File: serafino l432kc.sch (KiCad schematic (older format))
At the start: 28 parts

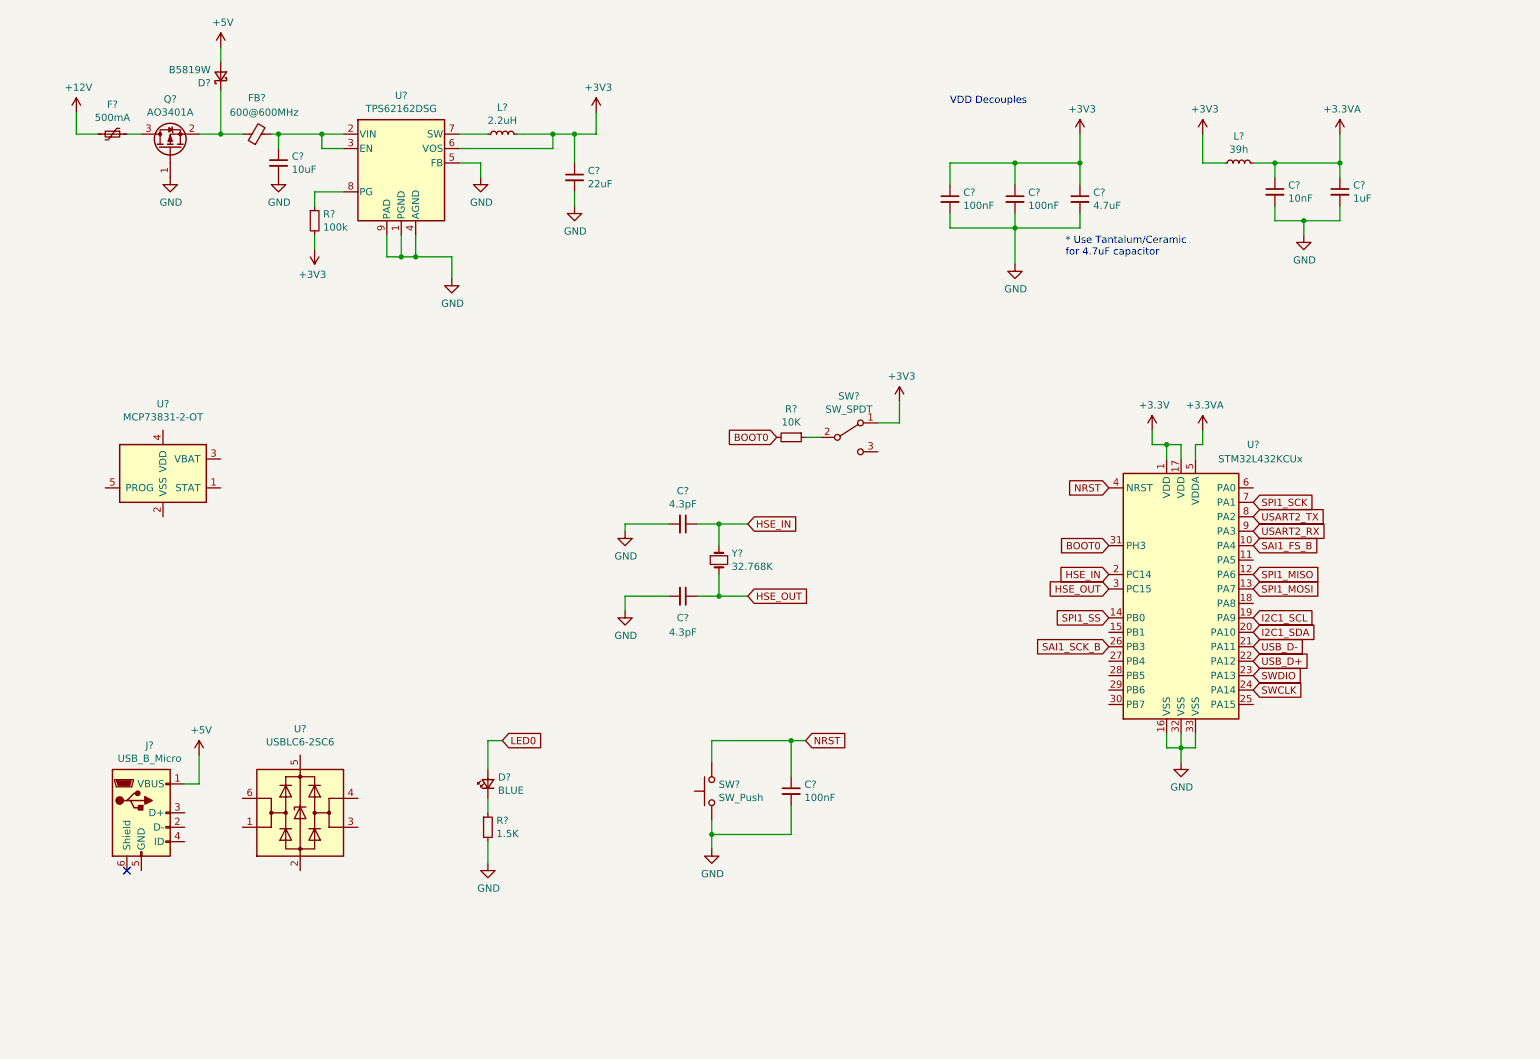
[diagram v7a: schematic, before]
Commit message: Upgrade to high effiency buck converter
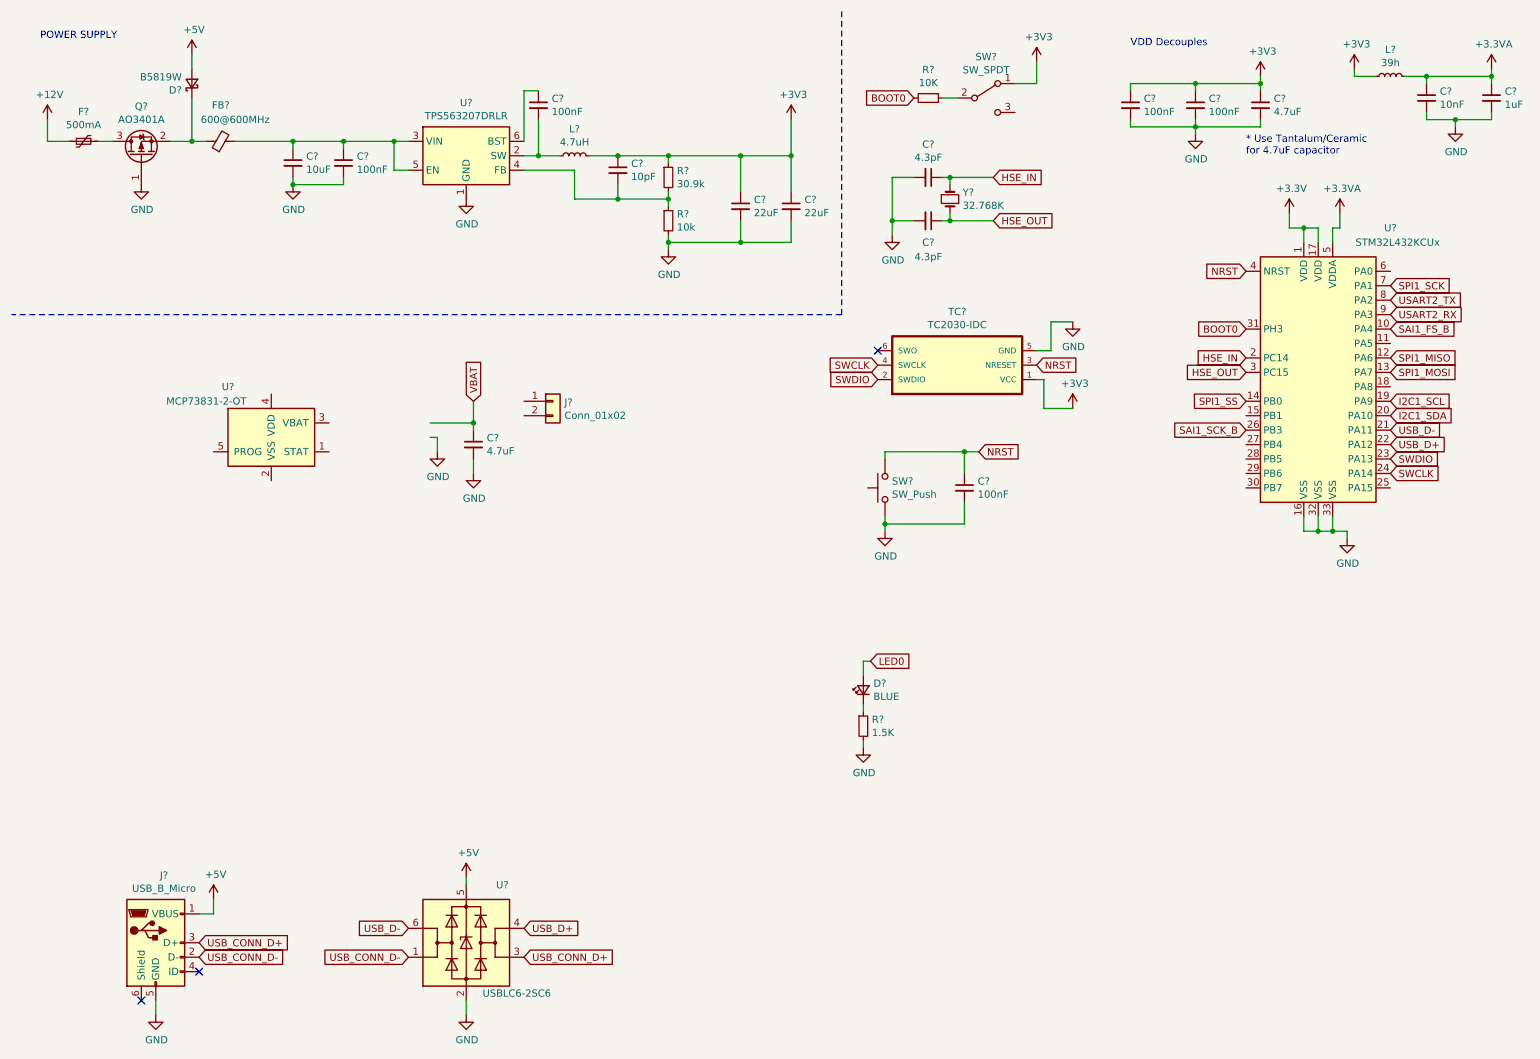
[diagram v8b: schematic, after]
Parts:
- removed C?: 10uF, symbol Device:C_Small
- removed C?: 22uF, symbol Device:C_Small
- removed L?: 2.2uH, symbol Device:L_Small
- removed R?: 100k, symbol Device:R_Small
- removed U?: TPS62162DSG, Package_SON:WSON-8-1EP_2x2mm_P0.5mm_EP0.9x1.6mm_ThermalVias, symbol Regulator_Switching:TPS62162DSG
- added C? (x2): 100nF, symbol Device:C_Small
- added C?: 10uF, symbol Device:C_Small
- added C?: 10pF, symbol Device:C_Small
- added C? (x2): 22uF, symbol Device:C_Small
- added C?: 4.7uF, symbol Device:C_Small
- added J?: Conn_01x02, symbol Connector_Generic:Conn_01x02
- added L?: 4.7uH, symbol Device:L_Small
- added R?: 30.9k, symbol Device:R_Small
- added R?: 10k, symbol Device:R_Small
- added TC?: TC2030-IDC, symbol TC2030-IDC:TC2030-IDC
- added U?: TPS563207DRLR, Package_TO_SOT_SMD:SOT-23-6, symbol TPS563207DRLR:TPS563207DRLR
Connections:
- net +3V3: now also C?.1, C?.1, C?.1, L?.2, R?.1, TC?.1 (VCC)
- net +5V: now also U?.5 (VBUS)
- net GND: now also J?.5 (GND), U?.2 (GND), C?.2, C?.2, C?.2, C?.2, C?.2, R?.2, TC?.5 (GND), U?.1 (GND)
- net NRST: now also TC?.3 (NRESET)
- net SWCLK: now also TC?.4 (SWCLK)
- net SWDIO: now also TC?.2 (SWDIO)
- net USB_D+: now also U?.4 (I/O2)
- net USB_D-: now also U?.6 (I/O1)
- net at FB?.2: now also C?.1, C?.1, U?.3 (VIN), U?.5 (EN)
- net USB_CONN_D-: now reaches J?.2 (D-)
- net USB_CONN_D-: now also U?.1 (I/O1)
- net USB_CONN_D+: now reaches J?.3 (D+)
- net USB_CONN_D+: now also U?.3 (I/O2)
- new net: C?.2, L?.1, U?.2 (SW)
- new net: C?.2, R?.1, R?.2, U?.4 (FB)
- new net: C?.1, U?.6 (BST)
- new net VBAT: C?.1
- no-connect marks 1 -> 3
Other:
- note added: "POWER SUPPLY"
- moved on the sheet: C?, D?, F?, FB?, J?, L?, Q?, R?, SW?, U?, Y?
